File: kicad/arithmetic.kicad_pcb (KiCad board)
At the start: 4 copper layers, 47.3 x 58.3 mm, 71 parts, among them J1 Conn_01x03_Male, J2 Conn_01x05_Male, J3 Conn_01x05_Male, J4 Conn_Coaxial, J5 Conn_Coaxial, J6 Conn_Coaxial, M2.5 MountingHole_2.7mm_M2.5_ISO73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, U1 LM317, U2 LM337, U3 OPA197xDBV, U4 OPA197xDBV, U5 OPA197xDBV

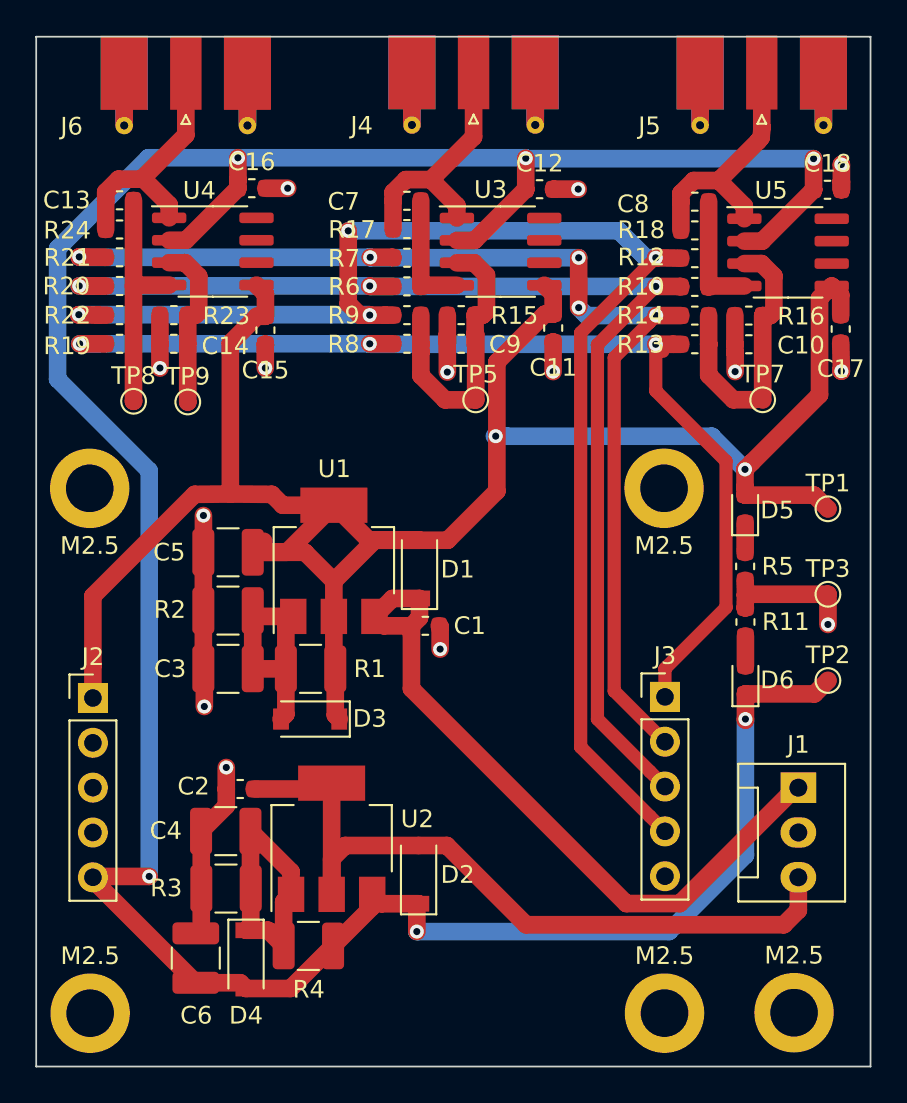
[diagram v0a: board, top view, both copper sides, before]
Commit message: applied ground-poor, via-stitching, added logo and rev to boards
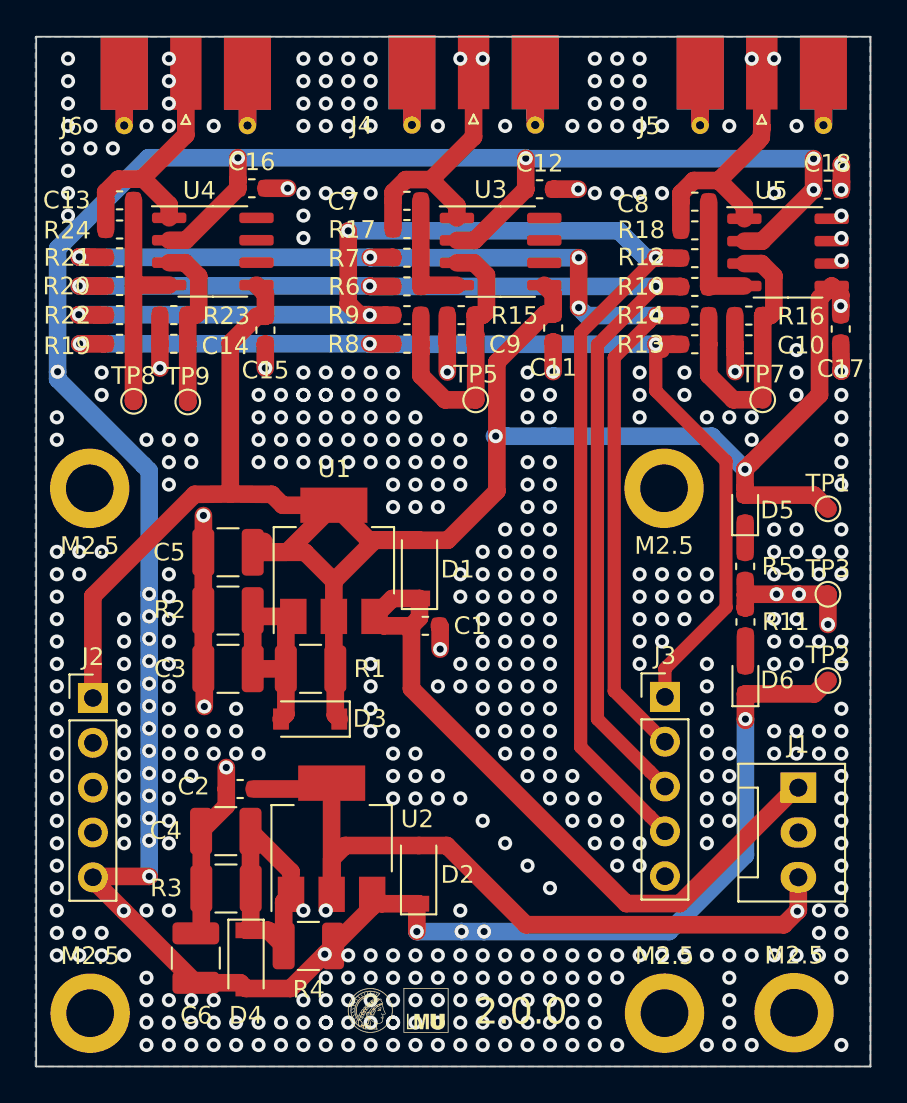
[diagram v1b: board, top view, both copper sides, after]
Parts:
- added G***: LOGO, Common:mpq_lmu_logo, F.Cu at (94.3, 132.7)
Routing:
- net +12V: vias 2 -> 3
- net Net-(C4-Pad2): vias 0 -> 1
- net GND: vias 14 -> 483
- net /DIFFY: vias 0 -> 2
- net /DIFFX: vias 0 -> 2
- net -15V: vias 0 -> 2
- net -12V: vias 6 -> 24
- net (no net): vias 0 -> 3
- added copper zone on B.Cu, net GND
- added copper zone on F.Cu, net GND
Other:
- board text added: "2.0.0"

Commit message: disabled fill zones, removed vias
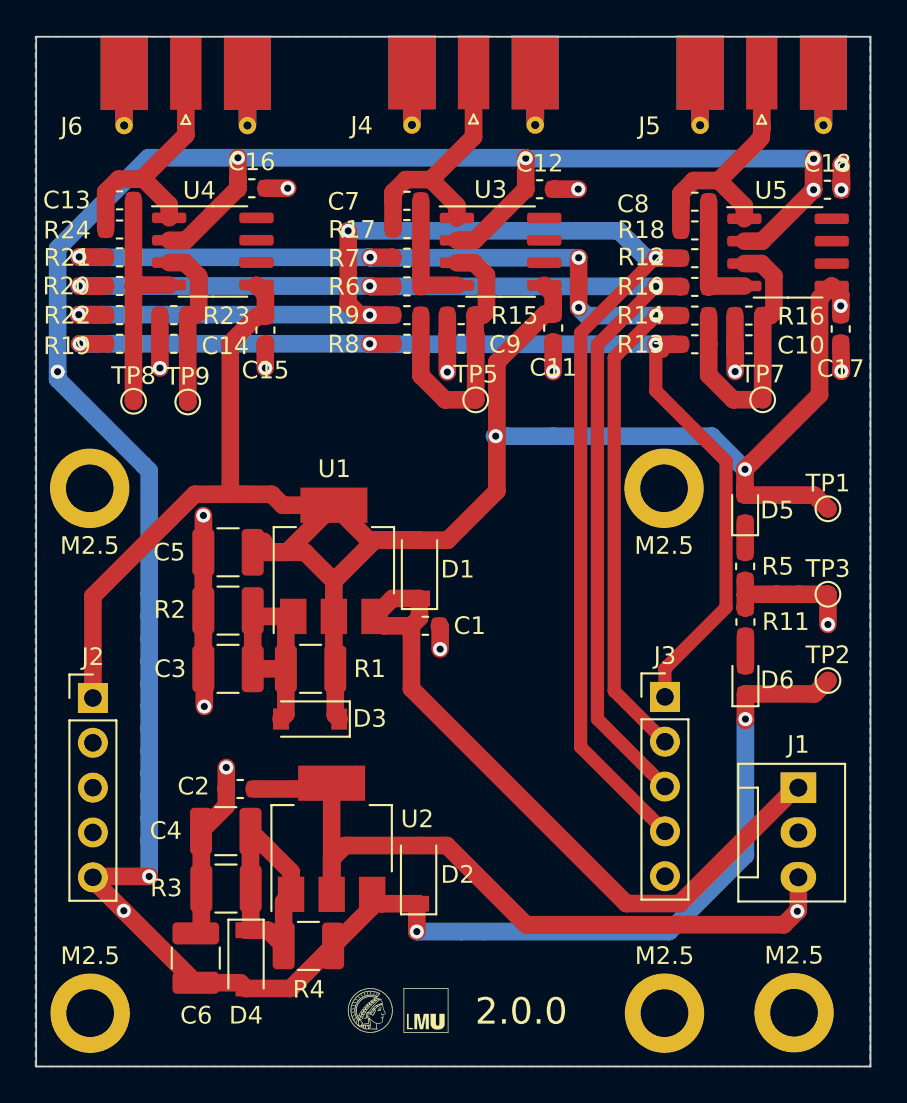
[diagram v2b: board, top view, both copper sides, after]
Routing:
- net Net-(C4-Pad2): vias 1 -> 0
- net GND: vias 483 -> 15
- net /DIFFY: vias 2 -> 0
- net /DIFFX: vias 2 -> 0
- net -15V: vias 2 -> 1
- net -12V: vias 24 -> 9
- net (no net): vias 3 -> 0
